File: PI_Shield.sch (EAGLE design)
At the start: 68 parts, among them Q1 220mA/50V/3.5Ω, Q3 220mA/50V/3.5Ω, Q4 220mA/50V/3.5Ω, Q5 2.5A/30V/105mΩ, U1 MAX1136EUA-T, U2 AZ1117EH-3.3TRG1, Y1 ECS-80-S-4X

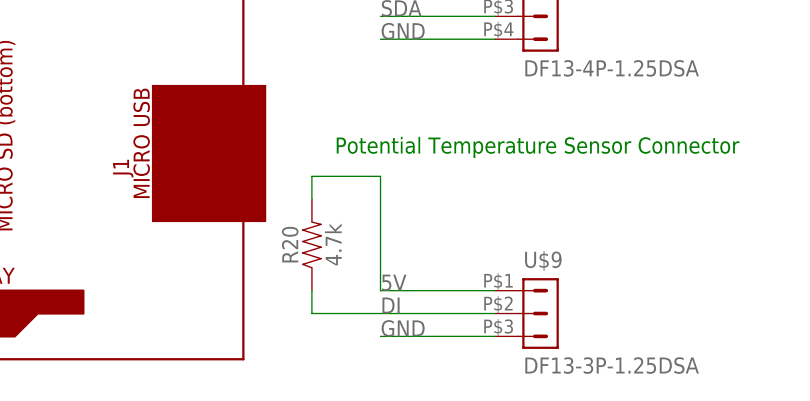
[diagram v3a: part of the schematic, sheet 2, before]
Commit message: switched power from 5v to 3.3v on dallas temperature sensor
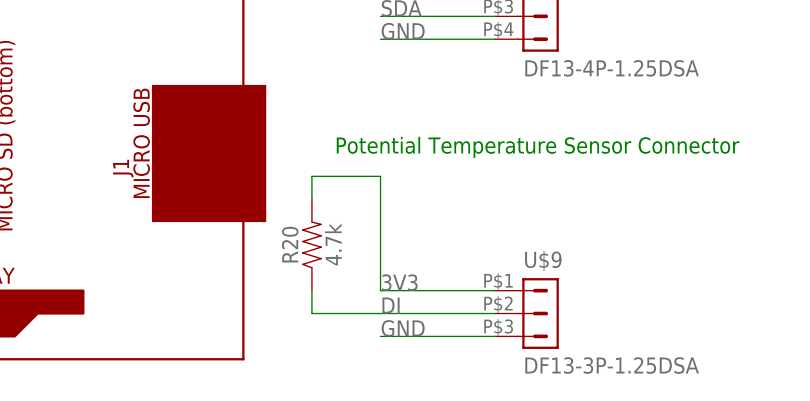
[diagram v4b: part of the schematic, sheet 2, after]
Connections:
- net 3V3: now also R20.2, U$9.1
- net 5V: no longer R20.2, U$9.1
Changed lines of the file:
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@@
-</segment>
-<segment>
-<pinref part="U$9" gate="G$1" pin="1"/>
-<wire x1="144.78" y1="17.78" x2="132.08" y2="17.78" width="0.1524" layer="91"/>
-<label x="132.08" y="17.78" size="1.778" layer="95"/>
-<pinref part="R20" gate="G$1" pin="2"/>
-<wire x1="124.46" y1="27.94" x2="124.46" y2="30.48" width="0.1524" layer="91"/>
-<wire x1="124.46" y1="30.48" x2="132.08" y2="30.48" width="0.1524" layer="91"/>
-<wire x1="132.08" y1="30.48" x2="132.08" y2="17.78" width="0.1524" layer="91"/>
 </segment>
 <segment>
@@
 <label x="231.14" y="78.74" size="1.778" layer="95"/>
 </segment>
+<segment>
+<pinref part="U$9" gate="G$1" pin="1"/>
+<wire x1="144.78" y1="17.78" x2="132.08" y2="17.78" width="0.1524" layer="91"/>
+<label x="132.08" y="17.78" size="1.778" layer="95"/>
+<pinref part="R20" gate="G$1" pin="2"/>
+<wire x1="124.46" y1="27.94" x2="124.46" y2="30.48" width="0.1524" layer="91"/>
+<wire x1="124.46" y1="30.48" x2="132.08" y2="30.48" width="0.1524" layer="91"/>
+<wire x1="132.08" y1="30.48" x2="132.08" y2="17.78" width="0.1524" layer="91"/>
+</segment>
 </net>
